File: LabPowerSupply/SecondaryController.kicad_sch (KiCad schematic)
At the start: 9 parts

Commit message: Finished first pass on the schematic
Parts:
- renumbered C1_Power to C1_Power1, C2_Power to C2_Power1, C3_Power to C3_Power1, C4_Power to C4_Power1, J_Boot to J_Boot1, R_Boot to R_Boot1, R_Reset to R_Reset1, SW_Reset to SW_Reset1, U_Secondary to U_Secondary1
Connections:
- net On/Off: now reaches U_Secondary1.16 (PA6)
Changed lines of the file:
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@@
+    (stroke (width 0) (type default) (color 0 0 0 0))
+  )
+  (wire (pts (xy 115.57 111.76) (xy 116.84 111.76))
     (stroke (width 0) (type default) (color 0 0 0 0))
   )
@@
     (effects (font (size 1.27 1.27)) (justify left))
   )
+  (hierarchical_label "On{slash}Off" (shape output) (at 116.84 111.76 0)
+    (effects (font (size 1.27 1.27)) (justify left))
+  )
   (symbol (lib_id "Device:R_US") (at 53.34 102.87 0) (unit 1)
     (in_bom yes) (on_board yes) (fields_autoplaced)
-    (property "Reference" "R_Boot" (id 0) (at 55.88 101.5999 0)
+    (property "Reference" "R_Boot1" (id 0) (at 55.88 101.5999 0)
       (effects (font (size 1.27 1.27)) (justify left))
     )
@@
   (symbol (lib_id "Connector:Conn_01x03_Male") (at 43.18 68.58 0) (unit 1)
     (in_bom yes) (on_board yes) (fields_autoplaced)
-    (property "Reference" "J_Boot" (id 0) (at 43.815 60.96 0))
+    (property "Reference" "J_Boot1" (id 0) (at 43.815 60.96 0))
     (property "Value" "Conn_01x03_Male" (id 1) (at 43.815 63.5 0))
     (property "Footprint" "Connector_PinSocket_2.54mm:PinSocket_1x03_P2.54mm_Vertical" (id 2) (at 43.18 68.58 0)
@@
   (symbol (lib_id "MCU_ST_STM32L1:STM32L100C6UxA") (at 100.33 99.06 0) (unit 1)
     (in_bom yes) (on_board yes)
-    (property "Reference" "U_Secondary" (id 0) (at 104.14 57.15 0)
+    (property "Reference" "U_Secondary1" (id 0) (at 104.14 57.15 0)
       (effects (font (size 1.27 1.27)) (justify left))
     )
@@
   (symbol (lib_id "Device:C") (at 128.27 69.85 0) (unit 1)
     (in_bom yes) (on_board yes) (fields_autoplaced)
-    (property "Reference" "C1_Power" (id 0) (at 132.08 68.5799 0)
+    (property "Reference" "C1_Power1" (id 0) (at 132.08 68.5799 0)
       (effects (font (size 1.27 1.27)) (justify left))
     )
@@
   (symbol (lib_id "Device:C") (at 132.08 76.2 0) (unit 1)
     (in_bom yes) (on_board yes) (fields_autoplaced)
-    (property "Reference" "C2_Power" (id 0) (at 135.89 74.9299 0)
+    (property "Reference" "C2_Power1" (id 0) (at 135.89 74.9299 0)
       (effects (font (size 1.27 1.27)) (justify left))
     )
@@
   (symbol (lib_id "Device:C") (at 135.89 82.55 0) (unit 1)
     (in_bom yes) (on_board yes) (fields_autoplaced)
-    (property "Reference" "C3_Power" (id 0) (at 139.7 81.2799 0)
+    (property "Reference" "C3_Power1" (id 0) (at 139.7 81.2799 0)
       (effects (font (size 1.27 1.27)) (justify left))
     )
@@
   (symbol (lib_id "Device:C") (at 139.7 88.9 0) (unit 1)
     (in_bom yes) (on_board yes) (fields_autoplaced)
-    (property "Reference" "C4_Power" (id 0) (at 143.51 87.6299 0)
+    (property "Reference" "C4_Power1" (id 0) (at 143.51 87.6299 0)
       (effects (font (size 1.27 1.27)) (justify left))
     )
@@
   (symbol (lib_id "Device:R_US") (at 68.58 58.42 0) (unit 1)
     (in_bom yes) (on_board yes) (fields_autoplaced)
-    (property "Reference" "R_Reset" (id 0) (at 71.12 57.1499 0)
+    (property "Reference" "R_Reset1" (id 0) (at 71.12 57.1499 0)
       (effects (font (size 1.27 1.27)) (justify left))
     )
@@
   (symbol (lib_id "Switch:SW_MEC_5G") (at 68.58 78.74 90) (unit 1)
     (in_bom yes) (on_board yes) (fields_autoplaced)
-    (property "Reference" "SW_Reset" (id 0) (at 69.85 77.4699 90)
+    (property "Reference" "SW_Reset1" (id 0) (at 69.85 77.4699 90)
       (effects (font (size 1.27 1.27)) (justify right))
     )

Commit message: started PCB
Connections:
- no-connect marks 6 -> 29
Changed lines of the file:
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@@
   (junction (at 105.41 139.7) (diameter 0) (color 0 0 0 0)
   )
+  (no_connect (at 115.57 132.08))
+  (no_connect (at 115.57 129.54))
+  (no_connect (at 115.57 127))
+  (no_connect (at 115.57 134.62))
+  (no_connect (at 115.57 124.46))
+  (no_connect (at 115.57 116.84))
+  (no_connect (at 115.57 114.3))
+  (no_connect (at 82.55 101.6))
+  (no_connect (at 82.55 99.06))
+  (no_connect (at 82.55 109.22))
+  (no_connect (at 82.55 106.68))
+  (no_connect (at 82.55 104.14))
+  (no_connect (at 82.55 121.92))
+  (no_connect (at 82.55 119.38))
+  (no_connect (at 82.55 116.84))
+  (no_connect (at 82.55 114.3))
+  (no_connect (at 82.55 124.46))
+  (no_connect (at 82.55 127))
+  (no_connect (at 82.55 129.54))
+  (no_connect (at 82.55 134.62))
+  (no_connect (at 82.55 132.08))
+  (no_connect (at 82.55 111.76))
   (no_connect (at 82.55 86.36))
   (no_connect (at 82.55 88.9))
@@
   (no_connect (at 82.55 73.66))
   (no_connect (at 82.55 78.74))
+  (no_connect (at 82.55 96.52))
   (wire (pts (xy 48.26 71.12) (xy 53.34 71.12))
     (stroke (width 0) (type default) (color 0 0 0 0))

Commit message: more work
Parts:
- added J_STLink2: Conn_01x03_Male, Connector_PinHeader_2.54mm:PinHeader_1x03_P2.54mm_Vertical, symbol Connector:Conn_01x03_Male
- renumbered C1_Power1 to C1_Power2, C2_Power1 to C2_Power2, C3_Power1 to C3_Power2, C4_Power1 to C4_Power2, J_Boot1 to J_Boot2, U_Secondary1 to MCU_2, R_Boot1 to R_Boot2, R_Reset1 to R_Reset2, SW_Reset1 to SW_Reset2
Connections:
- net GND: now also J_STLink2.3 (Pin_3)
- net at MCU_2.34 (PA13): now also J_STLink2.1 (Pin_1)
- net at MCU_2.37 (PA14): now also J_STLink2.2 (Pin_2)
- no-connect marks 29 -> 27
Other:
- moved on the sheet: C1_Power2, C2_Power2, C3_Power2, C4_Power2

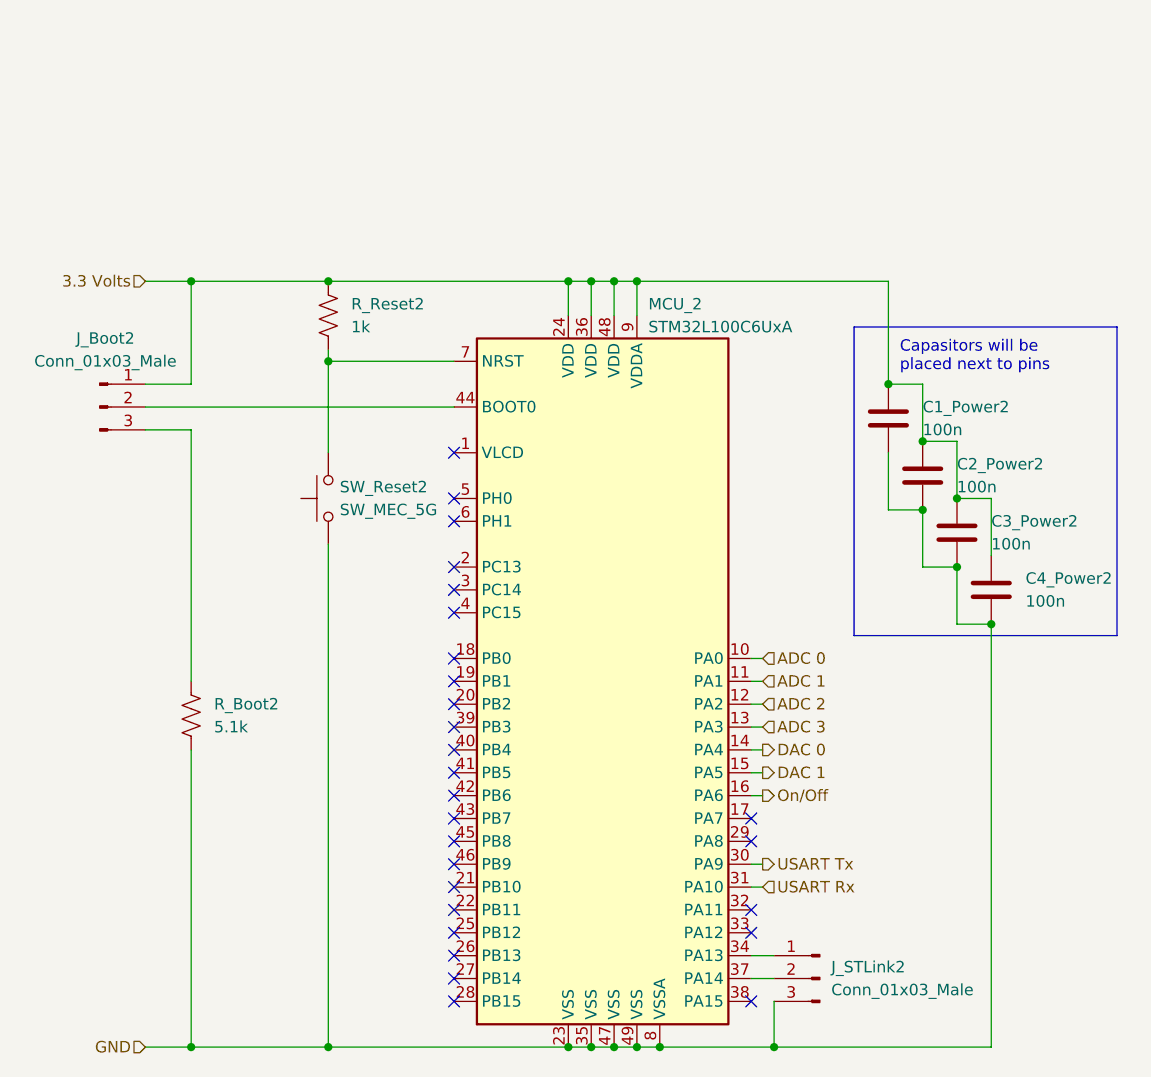
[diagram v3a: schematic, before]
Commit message: Resistor footprints changed to 0603
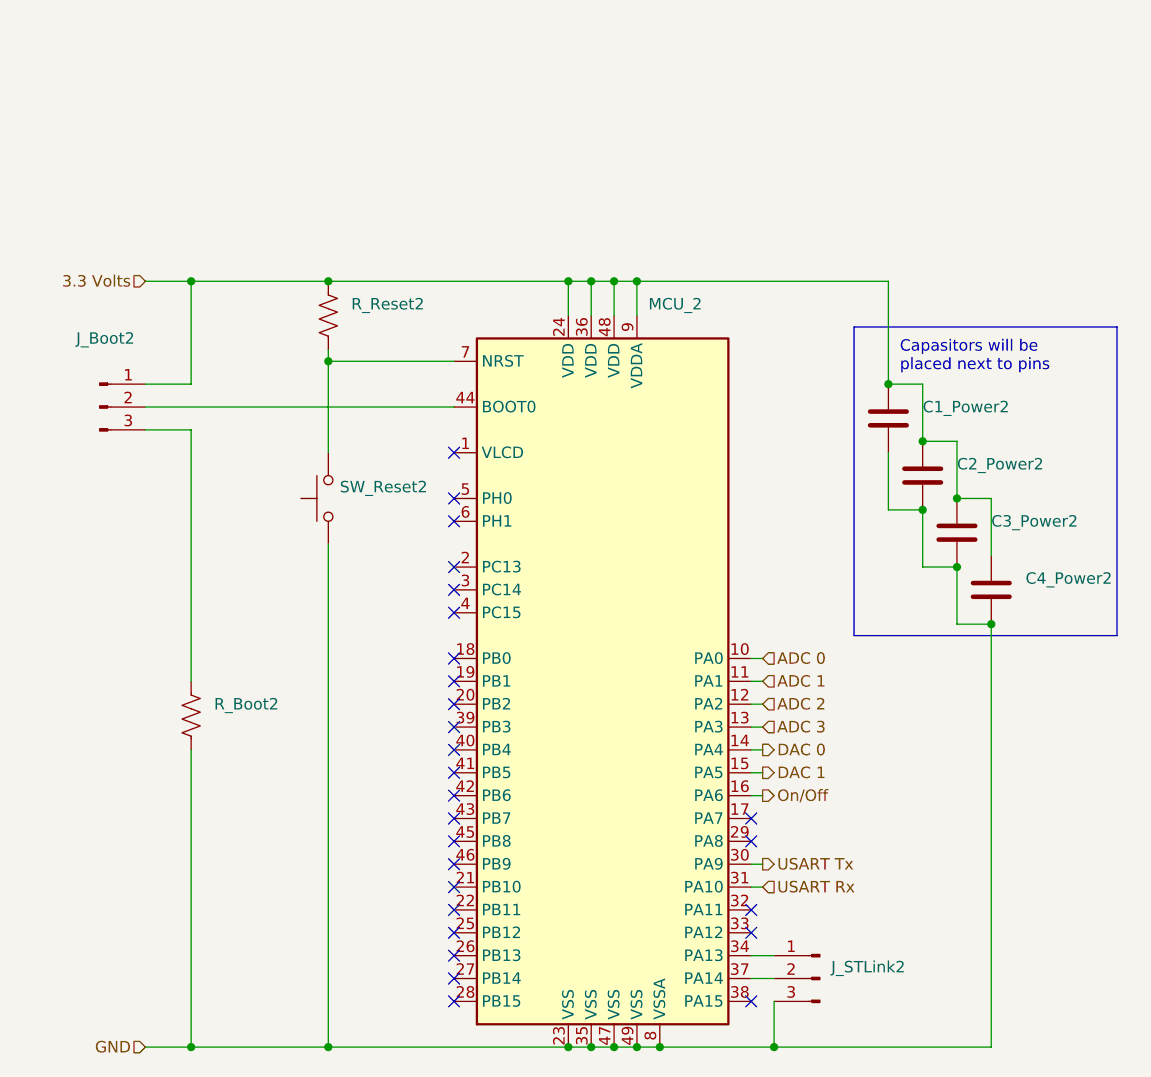
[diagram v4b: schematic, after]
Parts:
- C1_Power2, C2_Power2, C3_Power2, C4_Power2: value 100n -> (none); footprint Capacitor_SMD:C_1210_3225Metric -> (none)
- J_Boot2: value Conn_01x03_Male -> (none); footprint Connector_PinSocket_2.54mm:PinSocket_1x03_P2.54mm_Vertical -> (none)
- J_STLink2: value Conn_01x03_Male -> (none); footprint Connector_PinHeader_2.54mm:PinHeader_1x03_P2.54mm_Vertical -> (none)
- MCU_2: value STM32L100C6UxA -> (none); footprint Package_DFN_QFN:QFN-48-1EP_7x7mm_P0.5mm_EP5.6x5.6mm -> (none)
- R_Boot2: value 5.1k -> (none); footprint Resistor_SMD:R_1210_3225Metric -> (none)
- R_Reset2: value 1k -> (none); footprint Resistor_SMD:R_1210_3225Metric -> (none)
- SW_Reset2: value SW_MEC_5G -> (none); footprint Button_Switch_SMD:SW_MEC_5GSH9 -> (none)
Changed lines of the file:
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@@
       (effects (font (size 1.27 1.27)) (justify left))
     )
-    (property "Value" "5.1k" (id 1) (at 55.88 104.1399 0)
-      (effects (font (size 1.27 1.27)) (justify left))
-    )
-    (property "Footprint" "Resistor_SMD:R_1210_3225Metric" (id 2) (at 54.356 103.124 90)
+    (property "Value" "" (id 1) (at 55.88 104.1399 0)
+      (effects (font (size 1.27 1.27)) (justify left))
+    )
+    (property "Footprint" "" (id 2) (at 54.356 103.124 90)
       (effects (font (size 1.27 1.27)) hide)
     )
@@
     (in_bom yes) (on_board yes) (fields_autoplaced)
     (property "Reference" "J_Boot2" (id 0) (at 43.815 60.96 0))
-    (property "Value" "Conn_01x03_Male" (id 1) (at 43.815 63.5 0))
-    (property "Footprint" "Connector_PinSocket_2.54mm:PinSocket_1x03_P2.54mm_Vertical" (id 2) (at 43.18 68.58 0)
+    (property "Value" "" (id 1) (at 43.815 63.5 0))
+    (property "Footprint" "" (id 2) (at 43.18 68.58 0)
       (effects (font (size 1.27 1.27)) hide)
     )
@@
       (effects (font (size 1.27 1.27)) (justify left))
     )
-    (property "Value" "STM32L100C6UxA" (id 1) (at 104.14 59.69 0)
-      (effects (font (size 1.27 1.27)) (justify left))
-    )
-    (property "Footprint" "Package_DFN_QFN:QFN-48-1EP_7x7mm_P0.5mm_EP5.6x5.6mm" (id 2) (at 85.09 137.16 0)
+    (property "Value" "" (id 1) (at 104.14 59.69 0)
+      (effects (font (size 1.27 1.27)) (justify left))
+    )
+    (property "Footprint" "" (id 2) (at 85.09 137.16 0)
       (effects (font (size 1.27 1.27)) (justify right) hide)
     )
@@
       (effects (font (size 1.27 1.27)) (justify left))
     )
-    (property "Value" "100n" (id 1) (at 134.62 71.1199 0)
-      (effects (font (size 1.27 1.27)) (justify left))
-    )
-    (property "Footprint" "Capacitor_SMD:C_1210_3225Metric" (id 2) (at 131.7752 73.66 0)
+    (property "Value" "" (id 1) (at 134.62 71.1199 0)
+      (effects (font (size 1.27 1.27)) (justify left))
+    )
+    (property "Footprint" "" (id 2) (at 131.7752 73.66 0)
       (effects (font (size 1.27 1.27)) hide)
     )
@@
       (effects (font (size 1.27 1.27)) (justify right))
     )
-    (property "Value" "Conn_01x03_Male" (id 1) (at 124.46 133.3499 0)
-      (effects (font (size 1.27 1.27)) (justify right))
-    )
-    (property "Footprint" "Connector_PinHeader_2.54mm:PinHeader_1x03_P2.54mm_Vertical" (id 2) (at 123.19 132.08 0)
+    (property "Value" "" (id 1) (at 124.46 133.3499 0)
+      (effects (font (size 1.27 1.27)) (justify right))
+    )
+    (property "Footprint" "" (id 2) (at 123.19 132.08 0)
       (effects (font (size 1.27 1.27)) hide)
     )
@@
       (effects (font (size 1.27 1.27)) (justify left))
     )
-    (property "Value" "100n" (id 1) (at 138.43 77.4699 0)
-      (effects (font (size 1.27 1.27)) (justify left))
-    )
-    (property "Footprint" "Capacitor_SMD:C_1210_3225Metric" (id 2) (at 135.5852 80.01 0)
+    (property "Value" "" (id 1) (at 138.43 77.4699 0)
+      (effects (font (size 1.27 1.27)) (justify left))
+    )
+    (property "Footprint" "" (id 2) (at 135.5852 80.01 0)
       (effects (font (size 1.27 1.27)) hide)
     )
@@
       (effects (font (size 1.27 1.27)) (justify left))
     )
-    (property "Value" "100n" (id 1) (at 142.24 83.8199 0)
-      (effects (font (size 1.27 1.27)) (justify left))
-    )
-    (property "Footprint" "Capacitor_SMD:C_1210_3225Metric" (id 2) (at 139.3952 86.36 0)
+    (property "Value" "" (id 1) (at 142.24 83.8199 0)
+      (effects (font (size 1.27 1.27)) (justify left))
+    )
+    (property "Footprint" "" (id 2) (at 139.3952 86.36 0)
       (effects (font (size 1.27 1.27)) hide)
     )
@@
       (effects (font (size 1.27 1.27)) (justify left))
     )
-    (property "Value" "100n" (id 1) (at 146.05 90.1699 0)
-      (effects (font (size 1.27 1.27)) (justify left))
-    )
-    (property "Footprint" "Capacitor_SMD:C_1210_3225Metric" (id 2) (at 143.2052 92.71 0)
+    (property "Value" "" (id 1) (at 146.05 90.1699 0)
+      (effects (font (size 1.27 1.27)) (justify left))
+    )
+    (property "Footprint" "" (id 2) (at 143.2052 92.71 0)
       (effects (font (size 1.27 1.27)) hide)
     )
@@
       (effects (font (size 1.27 1.27)) (justify left))
     )
-    (property "Value" "1k" (id 1) (at 71.12 59.6899 0)
-      (effects (font (size 1.27 1.27)) (justify left))
-    )
-    (property "Footprint" "Resistor_SMD:R_1210_3225Metric" (id 2) (at 69.596 58.674 90)
+    (property "Value" "" (id 1) (at 71.12 59.6899 0)
+      (effects (font (size 1.27 1.27)) (justify left))
+    )
+    (property "Footprint" "" (id 2) (at 69.596 58.674 90)
       (effects (font (size 1.27 1.27)) hide)
     )
@@
       (effects (font (size 1.27 1.27)) (justify right))
     )
-    (property "Value" "SW_MEC_5G" (id 1) (at 69.85 80.0099 90)
-      (effects (font (size 1.27 1.27)) (justify right))
-    )
-    (property "Footprint" "Button_Switch_SMD:SW_MEC_5GSH9" (id 2) (at 63.5 78.74 0)
-      (effects (font (size 1.27 1.27)) hide)
-    )
+    (property "Value" "" (id 1) (at 69.85 80.0099 90)
+      (effects (font (size 1.27 1.27)) (justify right))
+    )
+    (property "Footprint" "" (id 2) (at 63.5 78.74 0)
+      (effects (font (size 1.27 1.27)) hide)
+    )

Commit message: Added mcu capacitors, split 5v inductors
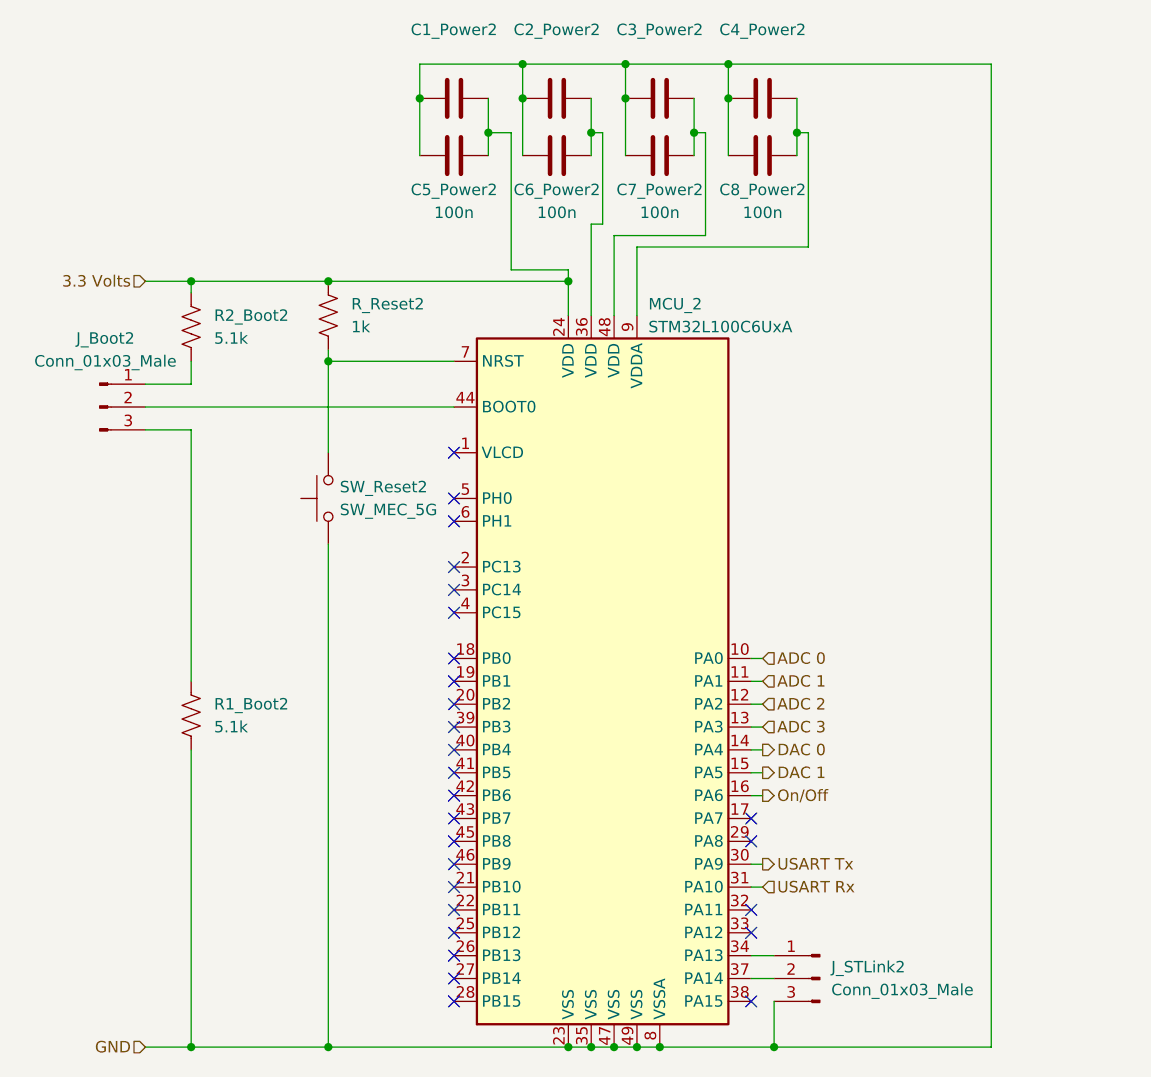
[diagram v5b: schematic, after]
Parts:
- added C5_Power2, C6_Power2, C7_Power2, C8_Power2: 100n, Capacitor_THT:C_Disc_D5.0mm_W2.5mm_P2.50mm, symbol Device:C
- added R2_Boot2: 5.1k, Resistor_SMD:R_0603_1608Metric, symbol Device:R_US
- C1_Power2, C2_Power2, C3_Power2, C4_Power2: footprint (none) -> Capacitor_THT:C_Disc_D5.0mm_W2.5mm_P2.50mm
- J_Boot2: value (none) -> Conn_01x03_Male; footprint (none) -> Connector_PinSocket_2.54mm:PinSocket_1x03_P2.54mm_Vertical
- J_STLink2: value (none) -> Conn_01x03_Male; footprint (none) -> Connector_PinHeader_2.54mm:PinHeader_1x03_P2.54mm_Vertical
- MCU_2: value (none) -> STM32L100C6UxA; footprint (none) -> Package_DFN_QFN:QFN-48-1EP_7x7mm_P0.5mm_EP5.6x5.6mm
- R1_Boot2: renamed from R_Boot2; value (none) -> 5.1k; footprint (none) -> Resistor_SMD:R_0603_1608Metric
- R_Reset2: value (none) -> 1k; footprint (none) -> Resistor_SMD:R_0603_1608Metric
- SW_Reset2: value (none) -> SW_MEC_5G; footprint (none) -> Button_Switch_SMD:SW_MEC_5GSH9
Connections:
- net 3.3 Volts: now also C1_Power2.2, C5_Power2.2, R2_Boot2.1; no longer C1_Power2.1, C2_Power2.1, C3_Power2.1, C4_Power2.1, J_Boot2.1 (Pin_1), MCU_2.36 (VDD), MCU_2.48 (VDD), MCU_2.9 (VDDA)
- net GND: now also C1_Power2.1, C2_Power2.1, C3_Power2.1, C4_Power2.1, C5_Power2.1, C6_Power2.1, C7_Power2.1, C8_Power2.1; no longer C1_Power2.2, C2_Power2.2, C3_Power2.2, C4_Power2.2
- new net: C4_Power2.2, C8_Power2.2, MCU_2.9 (VDDA)
- new net: J_Boot2.1 (Pin_1), R2_Boot2.2
- new net: C3_Power2.2, C7_Power2.2, MCU_2.48 (VDD)
- new net: C2_Power2.2, C6_Power2.2, MCU_2.36 (VDD)
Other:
- note removed: "Capasitors will be placed next to pins"
- moved on the sheet: C1_Power2, C2_Power2, C3_Power2, C4_Power2
